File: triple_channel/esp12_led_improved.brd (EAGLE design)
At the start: 50 x 37 mm, 30 parts

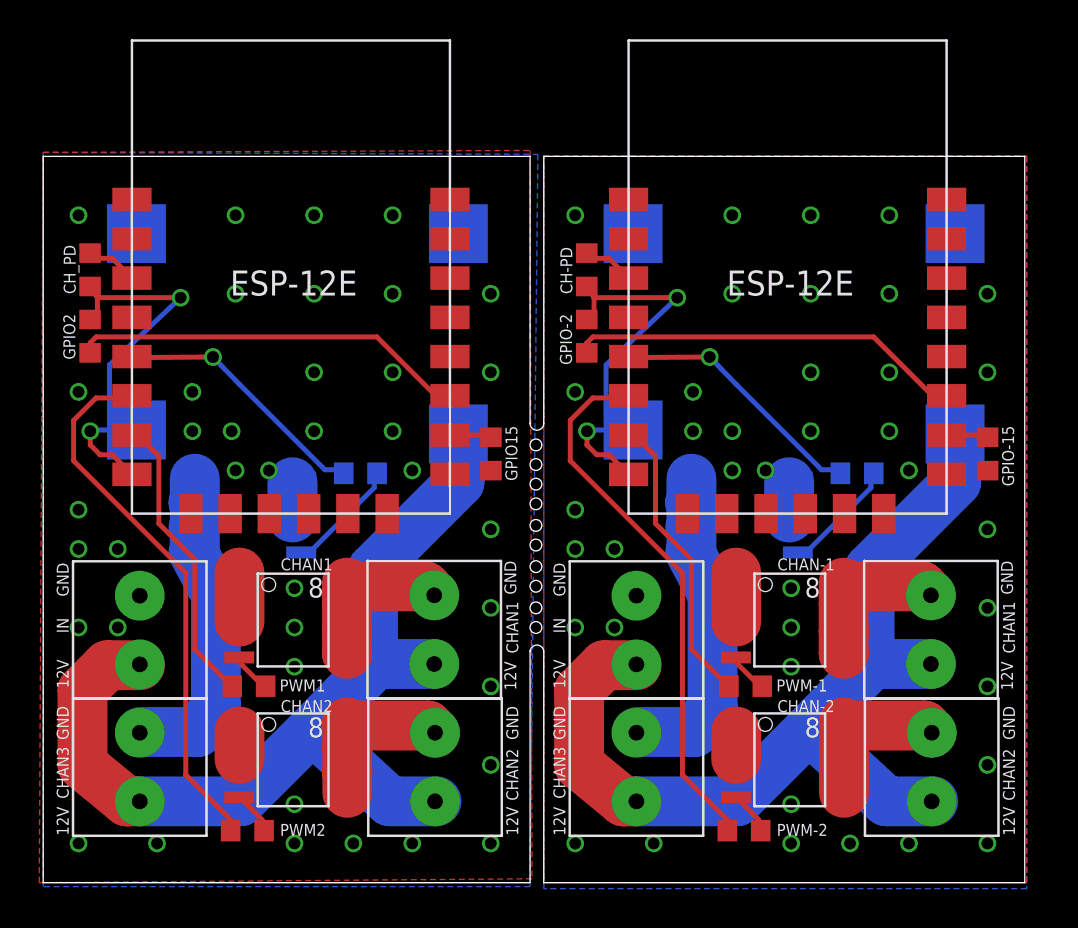
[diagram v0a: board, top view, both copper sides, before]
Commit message: Fixed PWM resistors being applied in series instead of as pulldowns
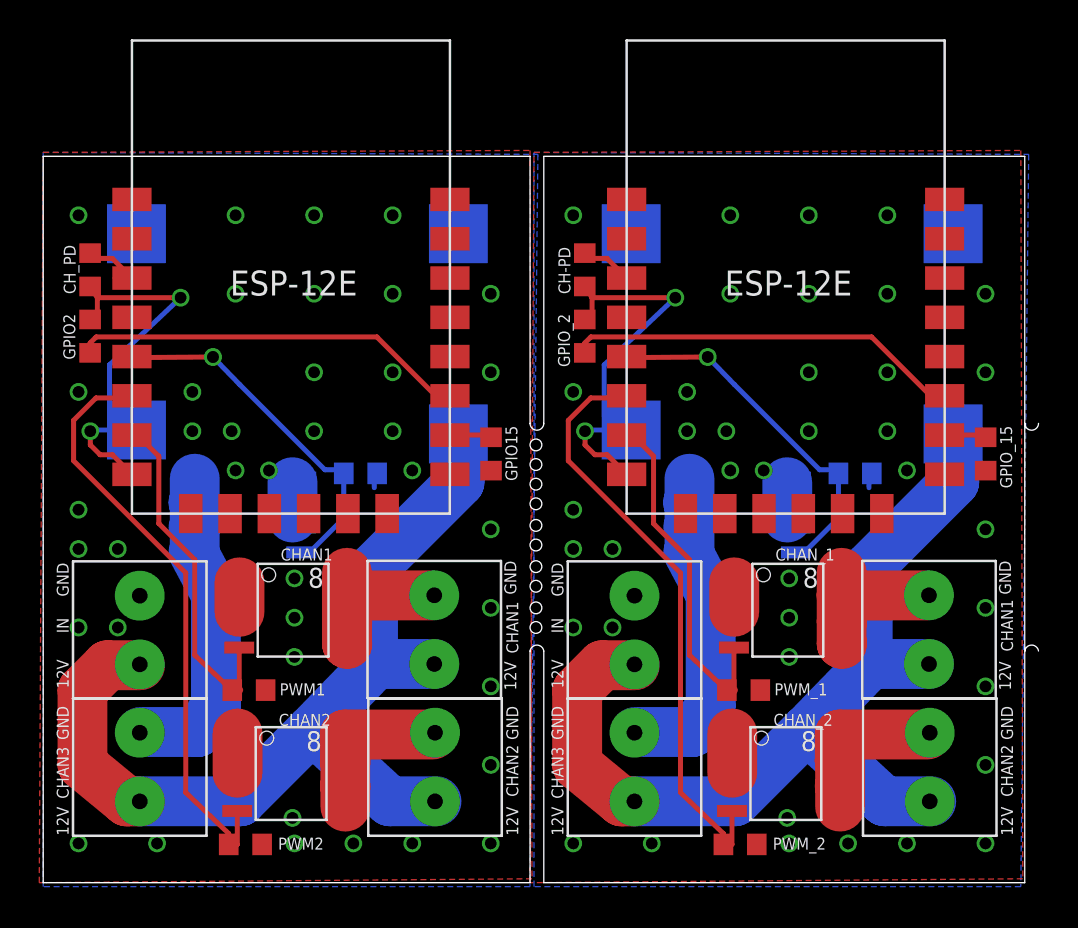
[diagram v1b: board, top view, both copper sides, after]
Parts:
- removed CHAN-1, CHAN-2, CHAN-3: (no value), transistor-fet:SO-8
- removed GPIO-15, GPIO-2, PWM-1, PWM-2, PWM-3: 10K, resistor:R0603
- added CHAN_1, CHAN_2, CHAN_3: (no value), transistor-fet:SO-8
- added GPIO_15, GPIO_2, PWM_1, PWM_2, PWM_3: 10K, resistor:R0603
- moved CHAN2 0.71 mm to (12.6, 5.56)
- moved PWM2 0.71 mm to (10.3, 1.95)
- moved CHAN1 0.50 mm to (12.7, 13.9)
- moved PWM1 0.20 mm to (10.5, 9.81)
- moved CH-PD 0.10 mm to (27.6, 31.2)
- moved OUT4 0.10 mm to (45.1, 12.9)
- moved OUT5 0.10 mm to (45.2, 5.89)
- moved PWR2 0.10 mm to (29.4, 33.6)
- moved OUT6 0.10 mm to (30.1, 5.89)
- moved PWR_IN1 0.10 mm to (30.1, 12.9)
- moved XXX1 0.10 mm to (37.3, 29.0)
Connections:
- removed net N$17: CHAN-2.5, CHAN-2.6, CHAN-2.7, CHAN-2.8, OUT5.2
- removed net N$18: CHAN-2.4, PWM-2.2
- removed net N$19: CHAN-3.5, CHAN-3.6, CHAN-3.7, CHAN-3.8, OUT6.2
- removed net N$20: CHAN-3.4, PWM-3.2
- removed net N$21: PWM-2.1, XXX1.6
- removed net N$22: PWM-3.1, XXX1.5
- net 3.3V1: now also GPIO_2.1; no longer GPIO-2.1
- net GND: now also PWM1.2, PWM2.2, PWM3.2
- net GND1: now also CHAN_1.1, CHAN_1.2, CHAN_1.3, CHAN_2.1, CHAN_2.2, CHAN_2.3, CHAN_3.1, CHAN_3.2, CHAN_3.3, GPIO_15.2, PWM_1.2, PWM_2.2, PWM_3.2; no longer CHAN-1.1, CHAN-1.2, CHAN-1.3, CHAN-2.1, CHAN-2.2, CHAN-2.3, CHAN-3.1, CHAN-3.2, CHAN-3.3, GPIO-15.2
- net N$10: now also CHAN_1.4, PWM_1.1, XXX1.7; no longer CHAN3.4, PWM3.2
- net N$11: now also CHAN2.4
- net N$12: now also CHAN3.4
- net N$13: now also CHAN_2.5, CHAN_2.6, CHAN_2.7, CHAN_2.8, OUT5.2; no longer CHAN-1.5, CHAN-1.6, CHAN-1.7, CHAN-1.8, OUT4.2
- net N$14: now also CHAN_3.5, CHAN_3.6, CHAN_3.7, CHAN_3.8, OUT6.2; no longer CHAN-1.4, PWM-1.2
- net N$15: now also CHAN_2.4, PWM_2.1, XXX1.6; no longer GPIO-2.2, XXX1.11
- net N$16: now also CHAN_3.4, PWM_3.1, XXX1.5; no longer PWM-1.1, XXX1.7
- net N$5: now also CHAN_1.5, CHAN_1.6, CHAN_1.7, CHAN_1.8, OUT4.2; no longer CHAN1.4, PWM1.2
- net N$6: now also CHAN1.4
- net N$8: now also GPIO_2.2, XXX1.11; no longer CHAN2.4, PWM2.2
- net S$4: now also GPIO_15.1; no longer GPIO-15.1
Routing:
- net N$21: track 27.8 -> 0.00 mm
- net N$8: track 2.23 -> 20.4 mm
- net N$19: track 17.4 -> 0.00 mm
- net N$14: track 2.34 -> 17.4 mm
- net N$22: track 13.4 -> 0.00 mm, vias 1 -> 0
- net N$10: track 5.94 -> 18.1 mm
- net N$15: track 20.4 -> 30.6 mm
- net N$17: track 8.95 -> 0.00 mm
- net N$5: track 2.34 -> 8.64 mm
- net N$20: track 5.94 -> 0.00 mm
- net N$12: track 13.4 -> 18.6 mm
- net N$16: track 15.2 -> 18.6 mm, vias 0 -> 1
- net N$6: track 15.2 -> 18.1 mm
- net N$11: track 27.8 -> 30.6 mm
- net N$18: track 2.23 -> 0.00 mm
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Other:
- board size 50 x 37 mm -> 50.7 x 37 mm

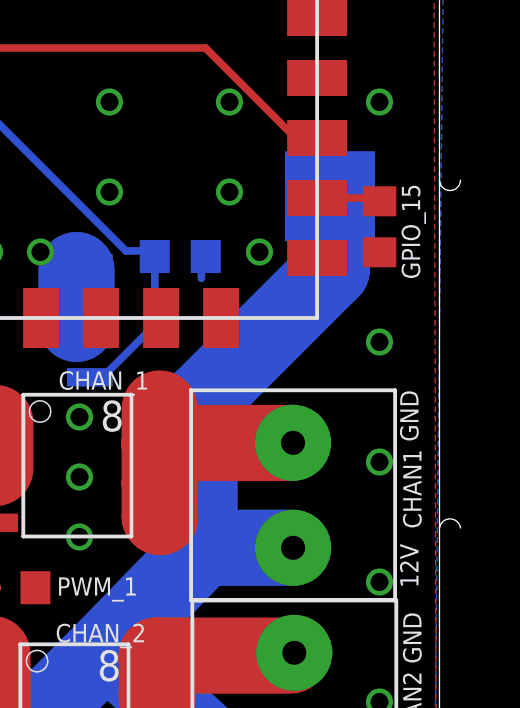
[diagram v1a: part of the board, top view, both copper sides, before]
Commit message: Fixed PWM resistors being applied in series instead of as pulldowns
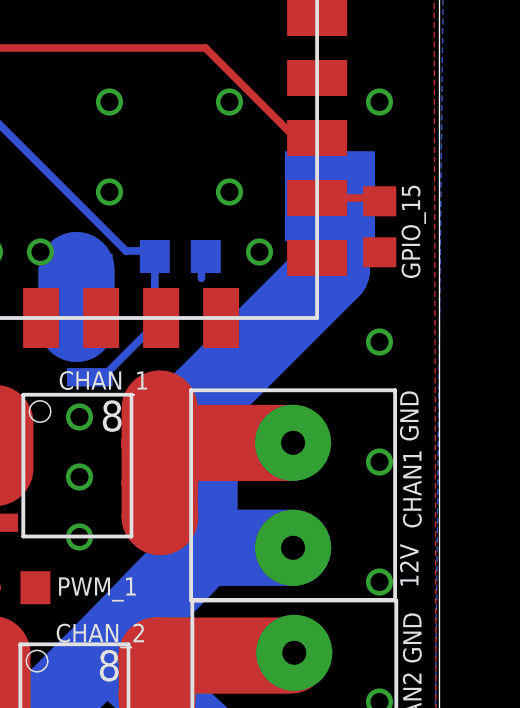
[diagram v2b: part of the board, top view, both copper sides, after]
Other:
- board size 50.7 x 37 mm -> 50 x 37 mm
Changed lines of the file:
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@@
 <wire x1="50" y1="37" x2="50" y2="23.4" width="0" layer="20"/>
 <wire x1="50" y1="11.8" x2="50" y2="0" width="0" layer="20"/>
-<wire x1="50" y1="11.8" x2="50.7" y2="11.8" width="0" layer="20" curve="-163.739795"/>
-<wire x1="50.7" y1="23.4" x2="50" y2="23.4" width="0" layer="20" curve="-180"/>
 <text x="26.5" y="13.1" size="0.6096" layer="25" rot="R90" align="bottom-center">IN</text>
 <text x="26.5" y="16.3" size="0.6096" layer="25" rot="R90" align="bottom-right">GND</text>
